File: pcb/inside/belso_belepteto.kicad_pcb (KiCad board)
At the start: 2 copper layers, 28 parts, among them J1 RJ12, Q1 IRF7103, SW1 SW_Push, U1 MP2348GTL-P

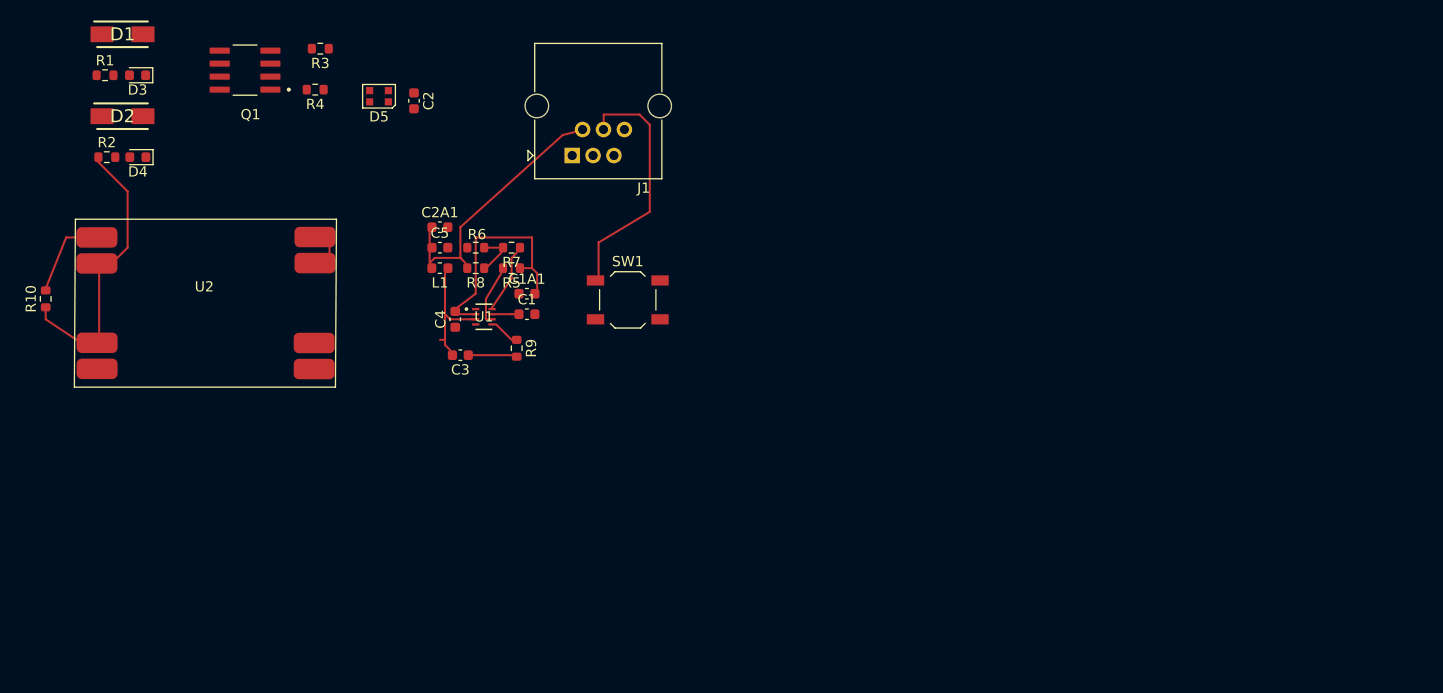
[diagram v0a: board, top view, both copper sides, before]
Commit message: schematic correction, layout improve
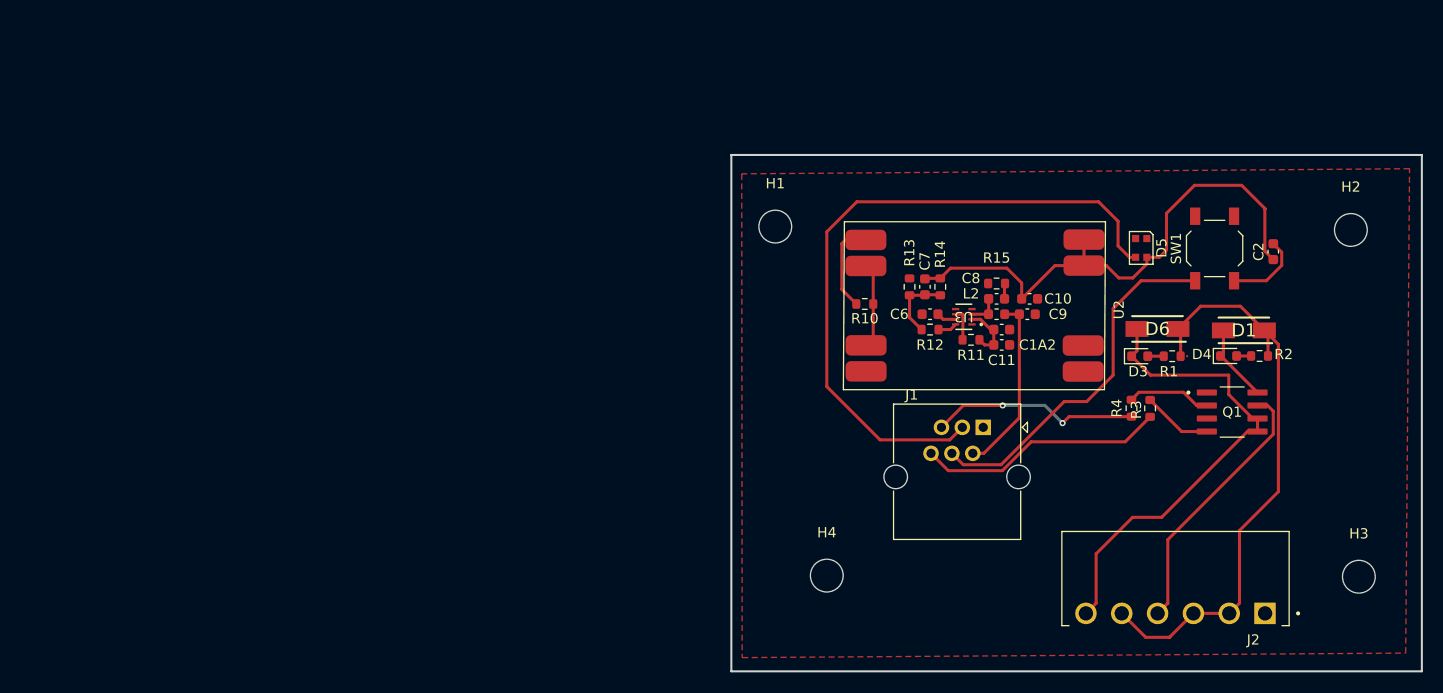
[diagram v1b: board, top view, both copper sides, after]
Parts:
- removed C1: 6.8nF, Capacitor_SMD:C_0603_1608Metric
- removed C1A1: 100nF, Capacitor_SMD:C_0603_1608Metric
- removed C2A1, C4, C5: 22uF, Capacitor_SMD:C_0603_1608Metric
- removed C3: 1uF, Capacitor_SMD:C_0603_1608Metric
- removed D2: SS34-HF, SS34-HF:DIOM5025X220N
- removed L1: 4.7uH, Inductor_SMD:L_0603_1608Metric
- removed R5: 604k, Resistor_SMD:R_0603_1608Metric
- removed R6: 7k68, Resistor_SMD:R_0603_1608Metric
- removed R7: 15k, Resistor_SMD:R_0603_1608Metric
- removed R8: 40k2, Resistor_SMD:R_0603_1608Metric
- removed R9: 15, Resistor_SMD:R_0603_1608Metric
- removed U1: MP2348GTL-P, footprints:SOT583_MP2348GTL_MNP
- added C10: 22uF, Capacitor_SMD:C_0603_1608Metric, F.Cu at (115.1, 54.0)
- added C11: 22uF, Capacitor_SMD:C_0603_1608Metric, F.Cu at (112.4, 58.5)
- added C1A2: 100nF, Capacitor_SMD:C_0603_1608Metric, F.Cu at (112.4, 57.0)
- added C6: 6.8nF, Capacitor_SMD:C_0603_1608Metric, F.Cu at (105.4, 55.5)
- added C7: 10pF, Capacitor_SMD:C_0603_1608Metric, F.Cu at (104.9, 52.8)
- added C8: 1uF, Capacitor_SMD:C_0603_1608Metric, F.Cu at (111.9, 54.0)
- added C9: 22uF, Capacitor_SMD:C_0603_1608Metric, F.Cu at (114.9, 55.5)
- added D6: D_Schottky, SS34-HF:DIOM5025X220N, F.Cu at (127.6, 56.9)
- added H1: MountingHole, MountingHole:MountingHole_3.2mm_M3, F.Cu at (90.3, 46.9)
- added H2: MountingHole, MountingHole:MountingHole_3.2mm_M3, F.Cu at (146.5, 47.3)
- added H3: MountingHole, MountingHole:MountingHole_3.2mm_M3, F.Cu at (147.3, 81.1)
- added H4: MountingHole, MountingHole:MountingHole_3.2mm_M3, F.Cu at (95.3, 81.0)
- added J2: Conn_01x06_Socket, Phoenix:CUI_TBP03R1-350-06BE, F.Cu at (138.1, 84.7)
- added L2: 4.7uH, Inductor_SMD:L_0603_1608Metric, F.Cu at (111.9, 55.5)
- added R11: 604k, Resistor_SMD:R_0603_1608Metric, F.Cu at (109.4, 58.0)
- added R12: 15k, Resistor_SMD:R_0603_1608Metric, F.Cu at (105.4, 57.0)
- added R13: 7k68, Resistor_SMD:R_0603_1608Metric, F.Cu at (103.4, 52.8)
- added R14: 40k2, Resistor_SMD:R_0603_1608Metric, F.Cu at (106.4, 52.8)
- added R15: 20, Resistor_SMD:R_0603_1608Metric, F.Cu at (111.9, 52.5)
- added U3: MP2348GTL-P, footprints:SOT583_MP2348GTL_MNP, F.Cu at (108.7, 55.7)
- D1: value SS34-HF -> D_Schottky
- moved R2 114.3 mm to (137.6, 59.6), turned to 180 degrees
- moved D1 113.3 mm to (136.0, 57.1), turned to 180 degrees
- moved D4 108.3 mm to (134.5, 59.6), turned to 0 degrees
- moved R1 107.8 mm to (129.0, 59.6), turned to 180 degrees
- moved Q1 102.0 mm to (134.9, 65.1), turned to 0 degrees
- moved D3 101.7 mm to (125.8, 59.6), turned to 0 degrees
- moved R3 88.3 mm to (126.9, 64.7), turned to 90 degrees
- moved R4 85.6 mm to (125.0, 64.7), turned to 90 degrees
- moved C2 85.2 mm to (138.9, 49.4), turned to 90 degrees
- moved R10 80.0 mm to (99.0, 54.5), turned to 180 degrees
- moved D5 75.9 mm to (126.0, 49.0), turned to -90 degrees
- moved U2 75.1 mm to (116.9, 72.9)
- moved SW1 57.5 mm to (133.2, 49.1), turned to 90 degrees
- moved J1 48.1 mm to (110.6, 66.5), turned to 0 degrees
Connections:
- net /In1 renamed /in1
- net /In2 renamed /in2
- C2 pad 1: Net-(D5-DOUT) -> +5V
- D1 pad 2: /out2 -> /out1
- D5 pad 1: Net-(D5-DOUT) -> unconnected-(D5-DOUT-Pad1)
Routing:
- net +12V: track 0.00 -> 72.4 mm
- net +5V: track 0.00 -> 70.2 mm
- net /led_in: track 0.00 -> 66.1 mm
- net /out2: track 0.00 -> 47.0 mm
- net Net-(J1-Pad4): track 0.00 -> 35.5 mm
- net /out1: track 0.00 -> 34.4 mm
- net /in2: track 0.00 -> 24.6 mm
- net /in1: track 0.00 -> 20.4 mm, vias 0 -> 2
- net Net-(U2-EN): track 0.00 -> 8.98 mm
- net Net-(Q1-Pad2): track 0.00 -> 8.20 mm
- net GND: track 0.00 -> 7.73 mm
- net Net-(C7-Pad1): track 0.00 -> 6.88 mm
- net Net-(Q1-Pad4): track 0.00 -> 6.82 mm
- net Net-(U3-EN): track 0.00 -> 3.20 mm
- net /sw: track 0.00 -> 3.14 mm
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- added copper zone on F.Cu, net GND
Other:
- board outline added: 67.4 x 50.4 mm
